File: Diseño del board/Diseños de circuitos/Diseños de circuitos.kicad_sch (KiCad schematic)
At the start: 4 parts

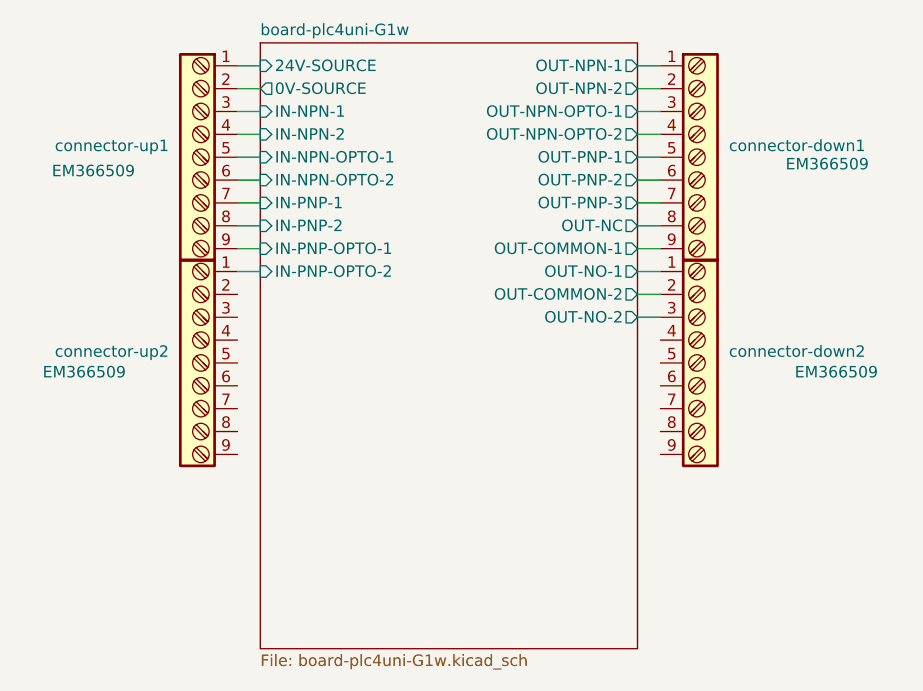
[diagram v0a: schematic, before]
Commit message: se agrego entrada y salida 0-10V
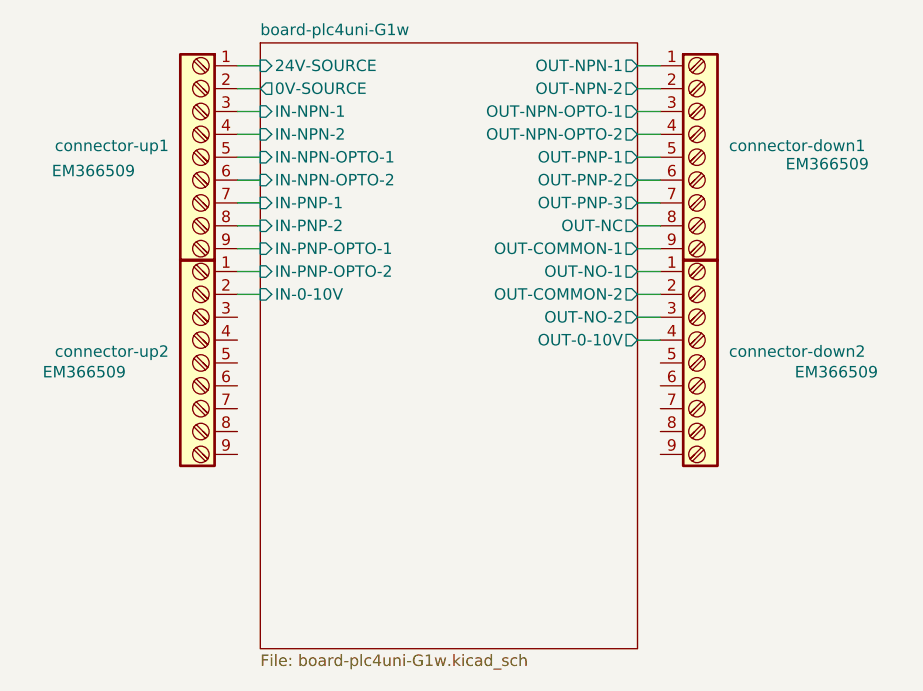
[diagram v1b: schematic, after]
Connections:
- net board-plc4uni-G1w/IN-0-10V: now reaches connector-up2.2
- net board-plc4uni-G1w/OUT-0-10V: now reaches connector-down2.4
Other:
- sheet board-plc4uni-G1w ports: added IN-0-10V, OUT-0-10V; removed none
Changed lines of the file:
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@@
+	(wire
+		(pts
+			(xy 111.76 74.93) (xy 114.3 74.93)
+		)
+		(stroke
+			(width 0)
+			(type default)
+		)
+	)
 	(wire
 		(pts
@@
 		(pts
 			(xy 156.21 67.31) (xy 158.75 67.31)
+		)
+		(stroke
+			(width 0)
+			(type default)
+		)
+	)
+	(wire
+		(pts
+			(xy 156.21 80.01) (xy 158.75 80.01)
 		)
 		(stroke
@@
 			(effects
 				(font
+					(size 1.27 1.27)
+				)
+				(justify right)
+			)
+		)
+		(pin "IN-0-10V" input
+			(at 114.3 74.93 180)
+			(effects
+				(font
+					(size 1.27 1.27)
+				)
+				(justify left)
+			)
+		)
+		(pin "OUT-0-10V" output
+			(at 156.21 80.01 0)
+			(effects
+				(font

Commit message: arreglos
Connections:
- no-connect marks 0 -> 12
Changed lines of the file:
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@@
 	(generator_version "9.0")
 	(paper "A4")
+	(no_connect
+		(at 111.76 80.01)
+	)
+	(no_connect
+		(at 158.75 82.55)
+	)
+	(no_connect
+		(at 158.75 90.17)
+	)
+	(no_connect
+		(at 111.76 90.17)
+	)
+	(no_connect
+		(at 158.75 87.63)
+	)
+	(no_connect
+		(at 111.76 87.63)
+	)
+	(no_connect
+		(at 111.76 92.71)
+	)
+	(no_connect
+		(at 111.76 77.47)
+	)
+	(no_connect
+		(at 158.75 85.09)
+	)
+	(no_connect
+		(at 158.75 92.71)
+	)
+	(no_connect
+		(at 111.76 82.55)
+	)
+	(no_connect
+		(at 111.76 85.09)
+	)
 	(wire
 		(pts
